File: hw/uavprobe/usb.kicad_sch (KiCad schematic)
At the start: 0 parts

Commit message: USB sheet
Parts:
- added C33, C36, C37: 100n, symbol Device:C
- added C34, C35: 12p, symbol Device:C
- added C38: 1u, symbol Device:C
- added D3: High-Speed, symbol Device:LED
- added D4: Suspend, symbol Device:LED
- added D5: USB host power, symbol Device:LED
- added D6: RP2040 power, symbol Device:LED
- added D7: USB peripheral power, symbol Device:LED
- added FL1: ECLAMP8052P.TCT, ECLAMP8052PTCT, symbol ECLAMP850:ECLAMP8052P.TCT
- added J17: USB_C_Receptacle_USB2.0_14P, symbol Connector:USB_C_Receptacle_USB2.0_14P
- added R10, R11, R13, R14, R15: 5.1k, symbol Device:R
- added R12: 10k, symbol Device:R
- added R16, R20, R21: 51k, symbol Device:R
- added R17, R22, R23, R24, R25: 75R, symbol Device:R
- added R18: 1M, symbol Device:R
- added R19: 12k, symbol Device:R
- added SW2: SW_Push, symbol Switch:SW_Push
- added U6: USB2412-DZK, USB2412-DZK:QFN50P500X500X100-29N, symbol USB2412:USB2412-DZK
- added Y2: 24MHz, symbol Device:Crystal_GND24
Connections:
- new net: R15.1, SW2.2
- new net: R19.2, U6.26 (RBIAS)
- new net: D5.1 (K), R23.1
- new net: R16.2, R17.2, U6.16 (HS_IND)
- new net: C34.1, R18.1, U6.23 (XTALOUT), Y2.1
- new net: C35.1, R18.2, U6.24 (XTALIN/CLKIN), Y2.3
- new net: C36.1, U6.25 (PLLFILT)
- new net: D3.1 (K), R17.1
- new net: FL1.1 (I/O+_IN), U6.3 (USBDP_DN2)
- new net: FL1.2 (I/O-_IN), U6.2 (USBDM_DN2)
- new net: D7.1 (K), R25.1
- new net: D4.1 (K), R22.1
- new net: R21.2, R22.2, U6.19 (SUSP_IND/NON_REM0)
- new net: J17.B5 (CC2), R10.1
- new net: R13.2, R14.2, U6.18 (VBUS_DET)
- new net: R20.1, U6.13 (NON_REM1)
- new net: J17.A7 (D-), J17.B7 (D-), U6.21 (USBDM_UP)
- new net: J17.A6 (D+), J17.B6 (D+), U6.22 (USBDP_UP)
- new net: C37.1, U6.9 (CRFILT)
- new net: D6.1 (K), R24.1
- new net: J17.A5 (CC1), R11.1
- new net +3.3V: C33.1, D3.2 (A), D4.2 (A), R12.2, R16.1, R21.1, U6.10 (VDD33), U6.14 (VDD33), U6.20 (VDD33), U6.27 (VDD33), U6.4 (VDD33)
- new net GND: C33.2, C34.2, C35.2, C36.2, C37.2, C38.2, FL1.3 (GND), J17.A1 (GND), J17.A12 (GND), J17.B1 (GND), J17.B12 (GND), J17.S1 (SHIELD), R10.2, R11.2, R14.1, R19.1, R20.2, R23.2, R24.2, R25.2, SW2.1, U6.15 (VSS), U6.29 (VSS), Y2.2, Y2.4
- new net USB1_D+: U6.1 (USBDP_DN1)
- new net USB1_D-: U6.28 (USBDM_DN1)
- new net USB2_D+: FL1.5 (I/O+_OUT)
- new net USB2_D-: FL1.4 (I/O-_OUT)
- new net VBUS: C38.1, D5.2 (A), J17.A4 (VBUS), J17.A9 (VBUS), J17.B4 (VBUS), J17.B9 (VBUS), R13.1
- new net VBUS1: D6.2 (A), U6.7 (PRTPWR1)
- new net VBUS2: D7.2 (A), U6.11 (PRTPWR2)
- new net ~{RESET}: R12.1, R15.2, U6.17 (~{RESET_IN})
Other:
- note added: "External oscillator"
- note added: "Indicators"
- note added: "NB: Update LED resistors after association!"
- note added: "Reset button"

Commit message: Cleanup and root sheet
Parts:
- renumbered C38 to C21, C36 to C22, C37 to C23, C33 to C24, C34 to C25, C35 to C26, J17 to J1, R15 to R10, R12 to R11, R11 to R12, R10 to R13, R13 to R14, R14 to R15, R18 to R16, R19 to R17, R20 to R18, R17 to R19, R16 to R20, R22 to R21, R21 to R22

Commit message: Power test points
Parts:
- added TP6: 3.3 V (HUB), symbol Connector:TestPoint_Probe
- added TP7: USB host power, symbol Connector:TestPoint_Probe
- added TP8: RP2040 power, symbol Connector:TestPoint_Probe
- added TP9: USB peripheral power, symbol Connector:TestPoint_Probe
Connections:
- net VBUS: now also TP7.1
- net VBUS1: now also TP8.1
- net VBUS2: now also TP9.1
- net +3.3V renamed +3.3V (HUB)
- net +3.3V (HUB): now also TP6.1

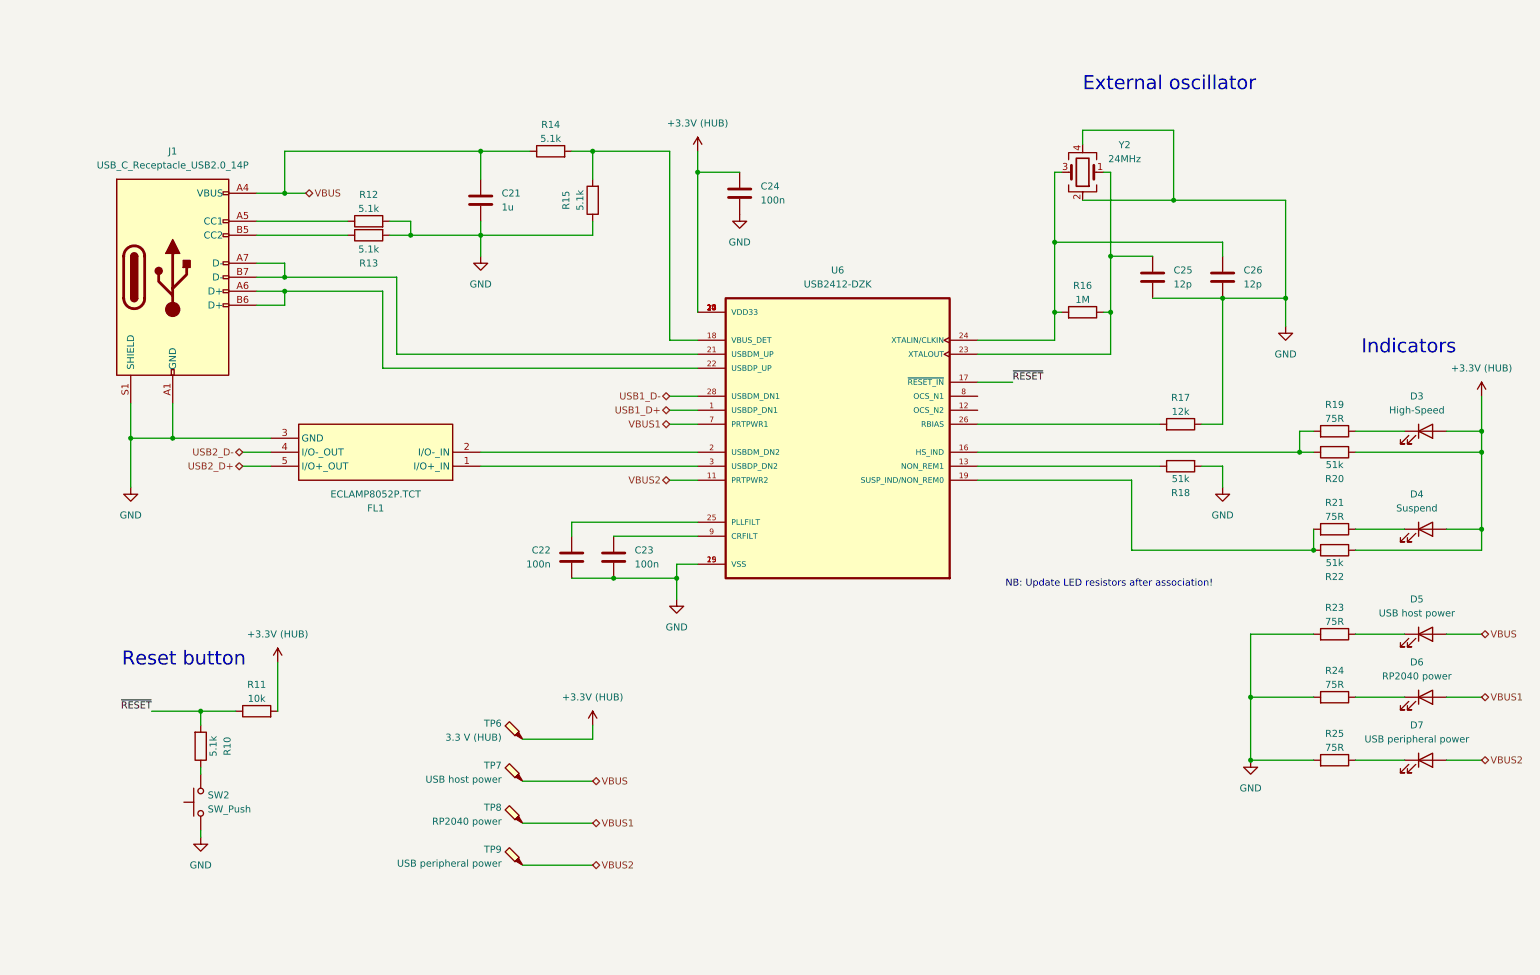
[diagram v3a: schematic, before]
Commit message: ERC pass
Footprint and symbol copy editing warnings left
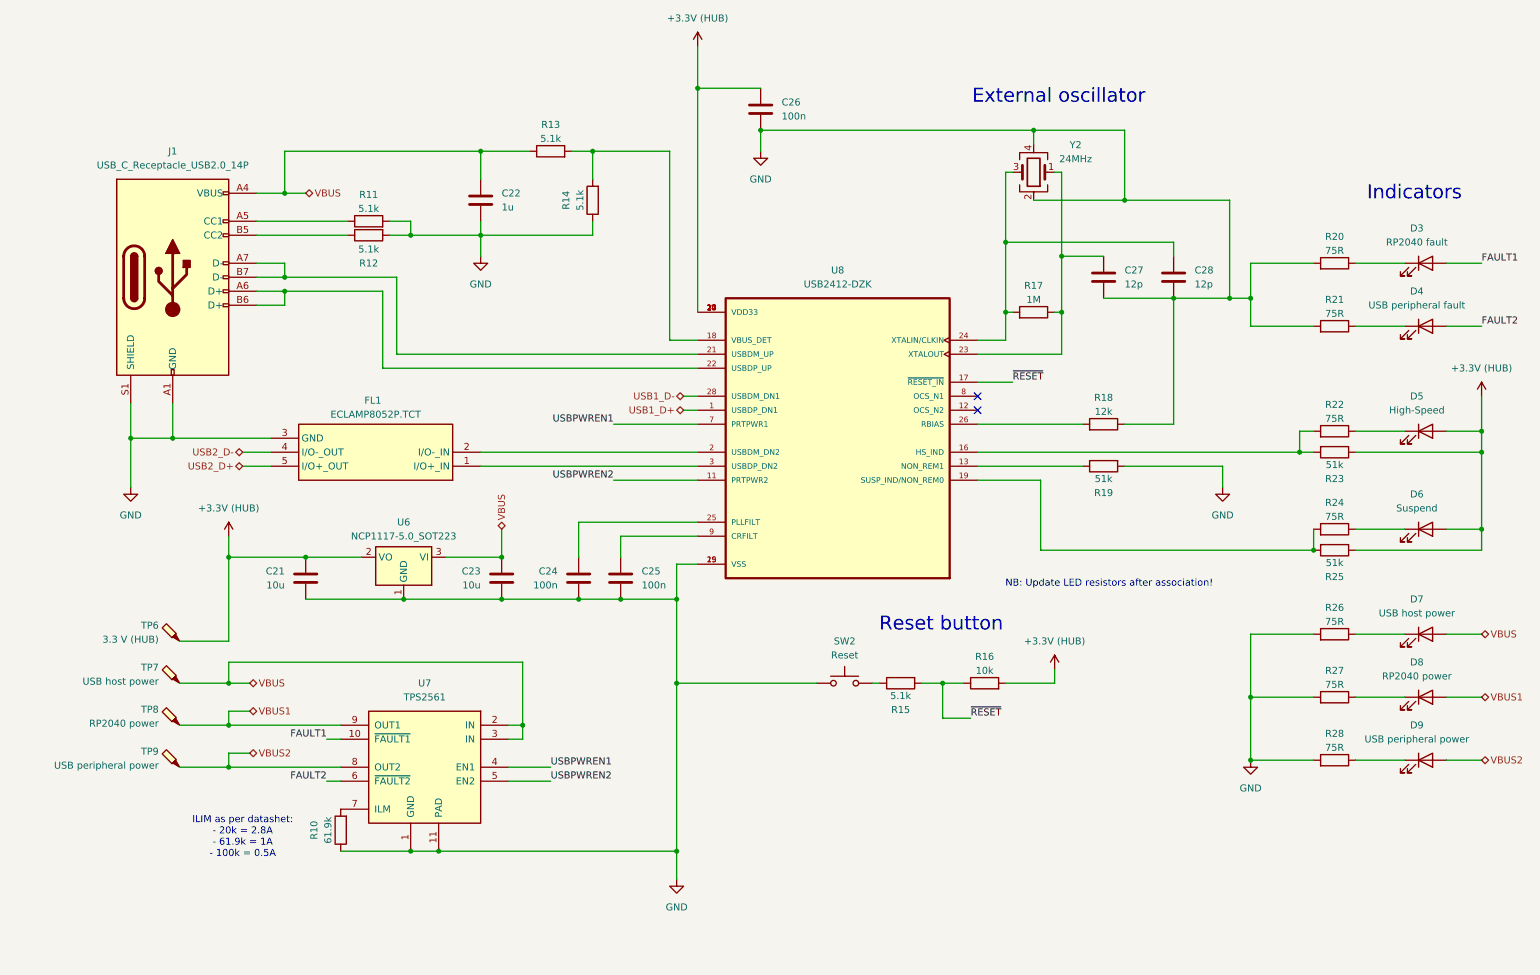
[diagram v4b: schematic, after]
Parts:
- added C21, C23: 10u, symbol Device:C
- added D3: RP2040 fault, symbol Device:LED
- added D4: USB peripheral fault, symbol Device:LED
- added R10: 61.9k, symbol Device:R
- added R20, R21: 75R, symbol Device:R
- added U6: NCP1117-5.0_SOT223, Package_TO_SOT_SMD:SOT-223-3_TabPin2, symbol Regulator_Linear:NCP1117-5.0_SOT223
- added U7: TPS2561, Package_SON:VSON-10-1EP_3x3mm_P0.5mm_EP1.65x2.4mm_ThermalVias, symbol Interface_USB:TPS2561
- SW2: value SW_Push -> Reset
- renumbered C21 to C22, C22 to C24, C23 to C25, C24 to C26, C25 to C27, C26 to C28, D3 to D5, D4 to D6, D5 to D7, D6 to D8, D7 to D9, R12 to R11, R13 to R12, R14 to R13, R15 to R14, R10 to R15, R11 to R16, R16 to R17, R17 to R18, R18 to R19, R19 to R22, R20 to R23, R21 to R24, R22 to R25, R23 to R26, R24 to R27, R25 to R28, U6 to U8
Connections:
- net +3.3V (HUB): now also C21.1, U6.2 (VO)
- net GND: now also C21.2, C23.2, R10.1, R20.2, R21.2, U6.1 (GND), U7.1 (GND), U7.11 (PAD)
- net VBUS: now also C23.1, U6.3 (VI), U7.2 (IN), U7.3 (IN)
- net VBUS1: now also U7.9 (OUT1); no longer U8.7 (PRTPWR1)
- net VBUS2: now also U7.8 (OUT2); no longer U8.11 (PRTPWR2)
- new net: D3.1 (K), R20.1
- new net: D4.1 (K), R21.1
- new net: R10.2, U7.7 (ILM)
- new net FAULT1: D3.2 (A), U7.10 (~{FAULT1})
- new net FAULT2: D4.2 (A), U7.6 (~{FAULT2})
- new net USBPWREN1: U7.4 (EN1), U8.7 (PRTPWR1)
- new net USBPWREN2: U7.5 (EN2), U8.11 (PRTPWR2)
- no-connect marks 0 -> 2
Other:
- note added: "ILIM as per datashet: - 20k = 2.8A - 61.9k = 1A - 100k = 0.5A"
- moved on the sheet: C24, C25, C26, C27, C28, R15, R16, R17, R18, R19, SW2, TP6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

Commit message: Footprint/MPN assignment pass
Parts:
- C21, C22, C23, C24, C25, C26, C27, C28: footprint (none) -> Capacitor_SMD:C_0402_1005Metric
- D3, D4: footprint (none) -> LED_SMD:LED_0402_1005Metric; MPN (none) -> QBLP595-R
- D5: footprint (none) -> LED_SMD:LED_0402_1005Metric; MPN (none) -> QBLP595-O
- D6: footprint (none) -> LED_SMD:LED_0402_1005Metric; MPN (none) -> QBLP595-Y
- D7: footprint (none) -> LED_SMD:LED_0402_1005Metric; MPN (none) -> QBLP595-IG
- D8: footprint (none) -> LED_SMD:LED_0402_1005Metric; MPN (none) -> QBLP595-AG
- D9: footprint (none) -> LED_SMD:LED_0402_1005Metric; MPN (none) -> QBLP595-IB
- FL1: footprint ECLAMP8052PTCT -> Import:ECLAMP8052PTCT; MPN (none) -> ECLAMP8052P.TCT; Manufacturer_Part_Number ECLAMP8052P.TCT -> (none)
- J1: footprint (none) -> Connector_USB:USB_C_Receptacle_GCT_USB4105-xx-A_16P_TopMnt_Horizontal; symbol Connector:USB_C_Receptacle_USB2.0_14P -> Connector:USB_C_Receptacle_USB2.0_16P; MPN (none) -> USB4105-GF-A
- R10, R11, R12, R13, R14, R15, R16, R17, R18, R19, R23, R25: footprint (none) -> Resistor_SMD:R_0402_1005Metric
- R20, R21, R27: value 75R -> 150R; footprint (none) -> Resistor_SMD:R_0402_1005Metric
- R22, R24: value 75R -> 10R; footprint (none) -> Resistor_SMD:R_0402_1005Metric
- R26, R28: value 75R -> 95R; footprint (none) -> Resistor_SMD:R_0402_1005Metric
- SW2: footprint (none) -> Button_Switch_SMD:SW_SPST_B3U-1000P; MPN (none) -> SW_SPST_B3U-1000P
- TP6, TP7, TP8, TP9: footprint (none) -> TestPoint:TestPoint_Pad_D1.5mm
- U6: MPN (none) -> NCP1117-5.0_SOT223
- U7: MPN (none) -> TPS2561
- U8: footprint USB2412-DZK:QFN50P500X500X100-29N -> Import:QFN50P500X500X100-29N; MP USB2412-DZK -> (none); MPN (none) -> USB2412-DZK
- Y2: footprint (none) -> Crystal:Crystal_SMD_Abracon_ABM3B-4Pin_5.0x3.2mm; MPN (none) -> ABM3B-24.000MHZ-10-B-1-U-T
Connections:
- net FAULT1: now also D3.1 (K); no longer D3.2 (A)
- net FAULT2: now also D4.1 (K); no longer D4.2 (A)
- net GND: no longer R20.2, R21.2
- net VBUS: now also R20.2, R21.2
- net at R20.1: now also D3.2 (A); no longer D3.1 (K)
- net at R21.1: now also D4.2 (A); no longer D4.1 (K)
- no-connect marks 2 -> 4
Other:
- moved on the sheet: D3, D4

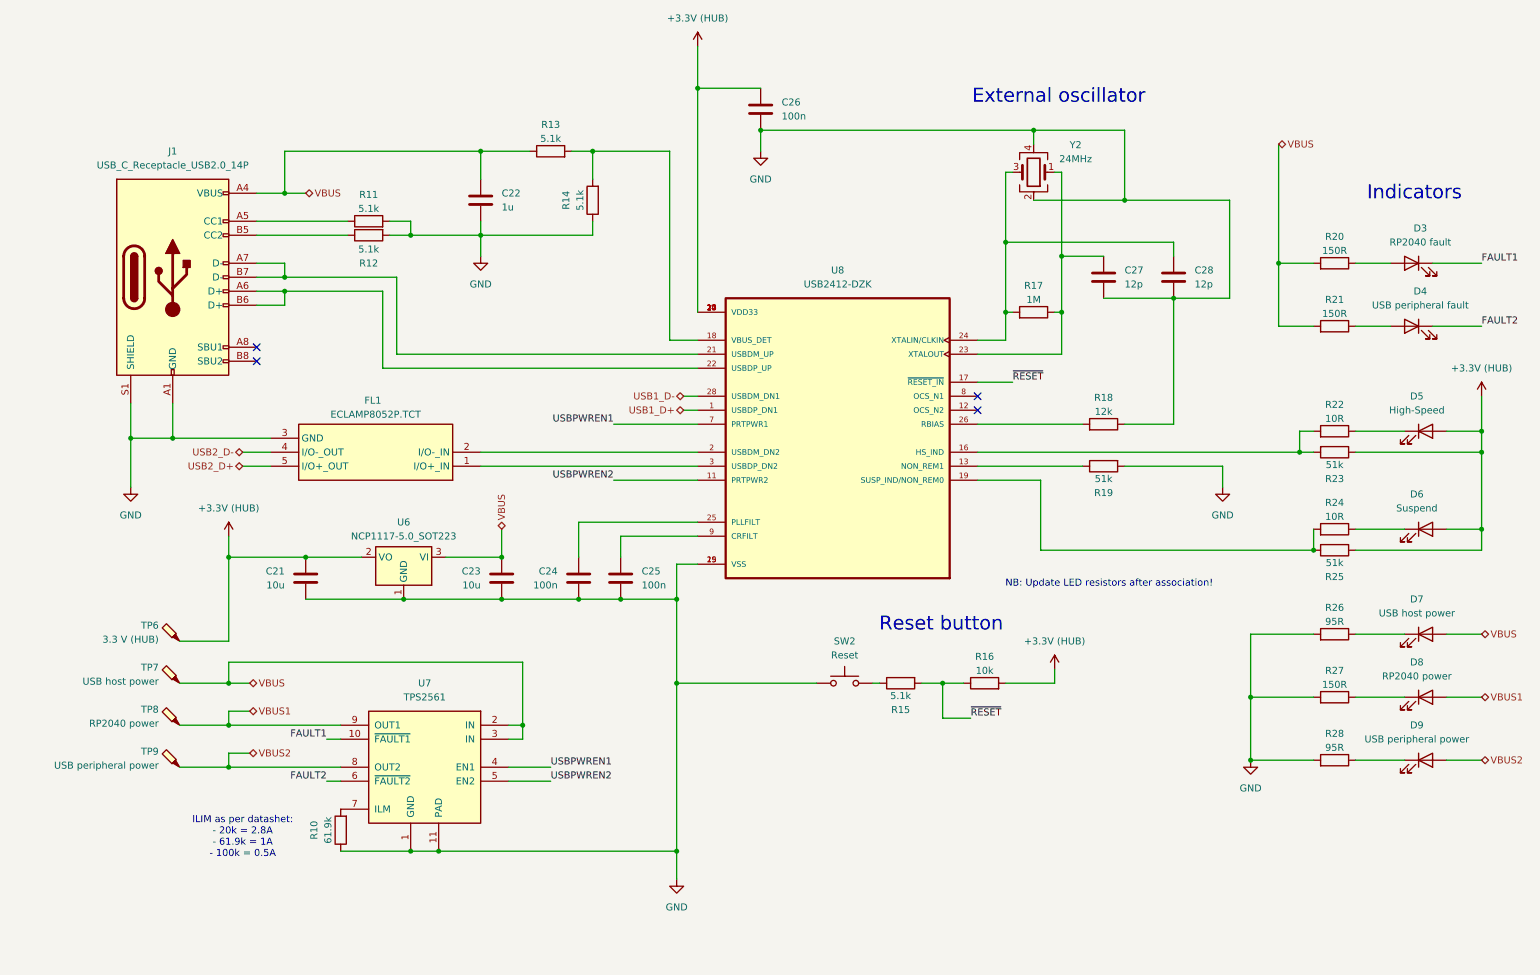
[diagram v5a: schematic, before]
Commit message: Design rules and net classes
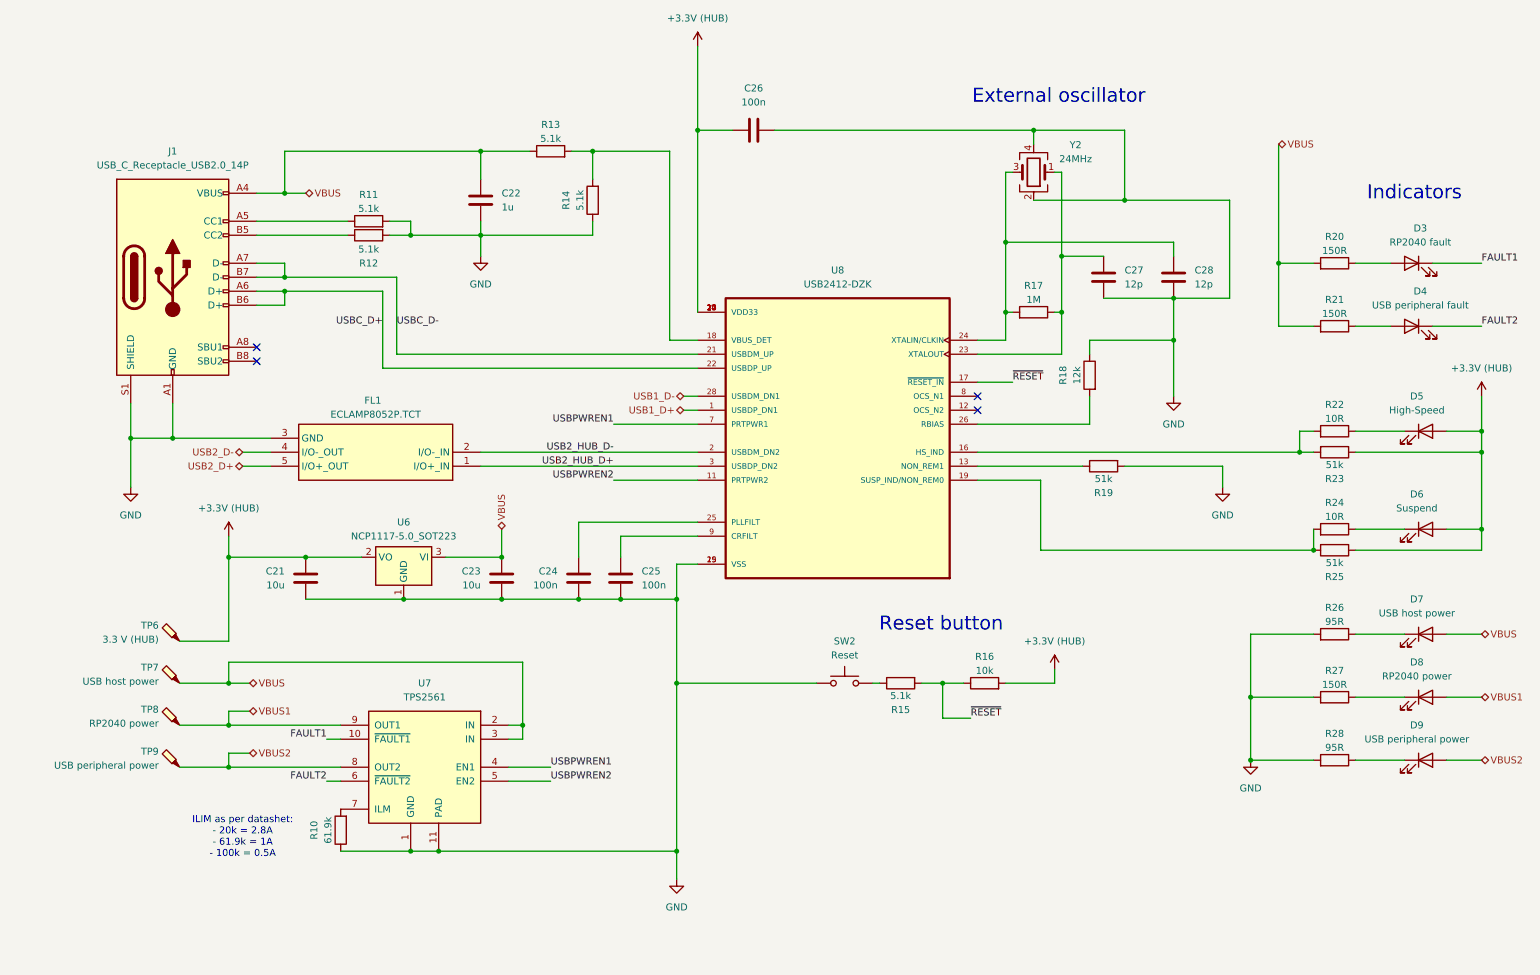
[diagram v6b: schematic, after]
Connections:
- net USB2_HUB_D+: now reaches FL1.1 (I/O+_IN), U8.3 (USBDP_DN2)
- net USB2_HUB_D-: now reaches FL1.2 (I/O-_IN), U8.2 (USBDM_DN2)
- net USBC_D-: now reaches J1.A7 (D-), J1.B7 (D-), U8.21 (USBDM_UP)
- net USBC_D+: now reaches J1.A6 (D+), J1.B6 (D+), U8.22 (USBDP_UP)
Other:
- note removed: "NB: Update LED resistors after association!"
- moved on the sheet: C26, R18
